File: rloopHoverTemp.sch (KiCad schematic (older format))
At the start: 26 parts, among them P1 CONN_01X02, P2 CONN_01X02, P3 CONN_01X01, P4 CONN_01X01, Q1 Q_NPN_BEC, Q2 Q_NPN_BEC, U1 XTR117, U2 TS305-10C50, U3 LTC2054, U4 XTR117, U5 LTC2054

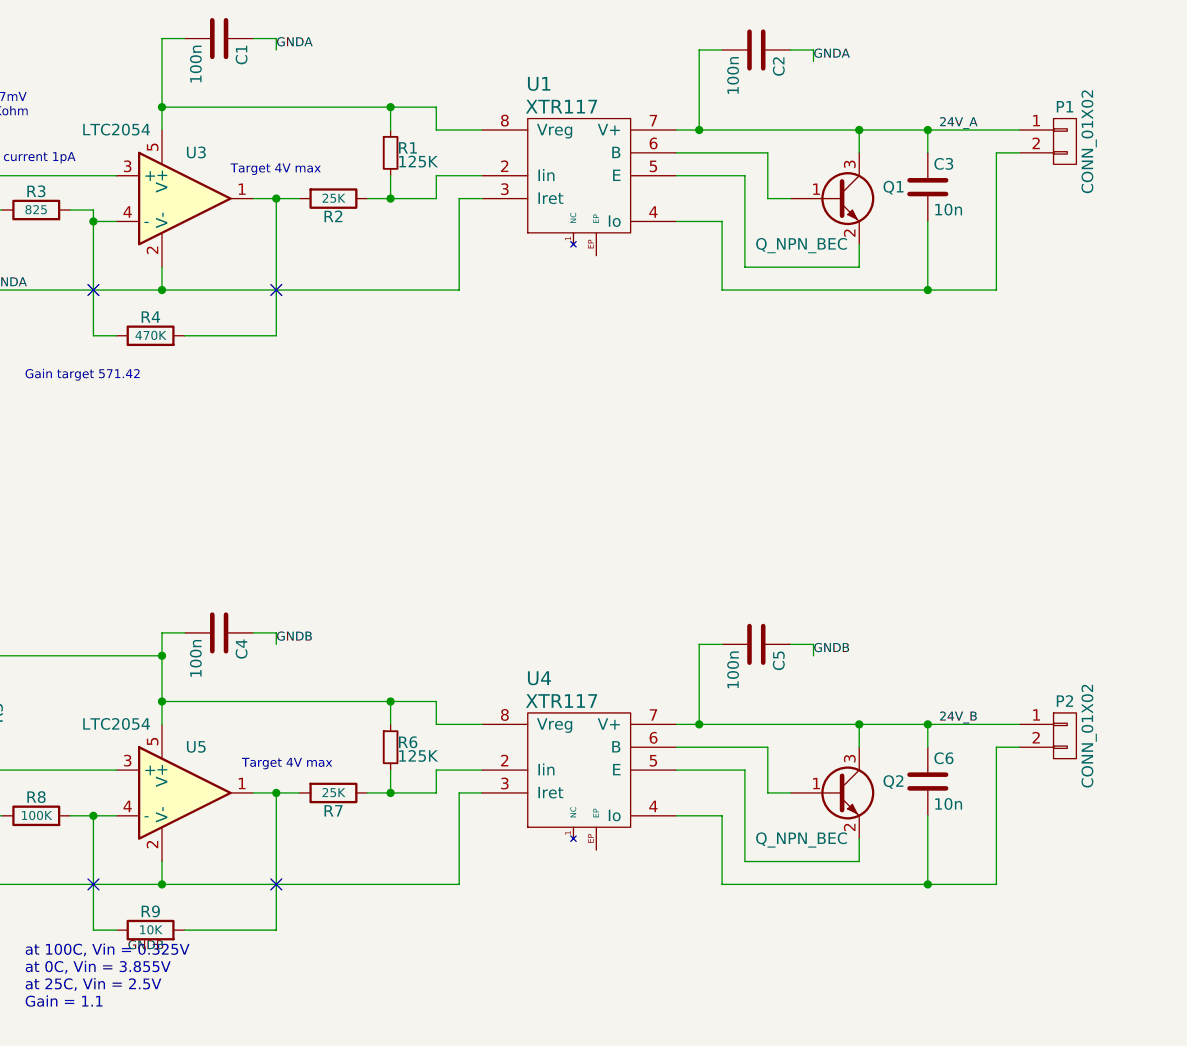
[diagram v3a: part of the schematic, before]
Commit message: added reverse wiring protection diode
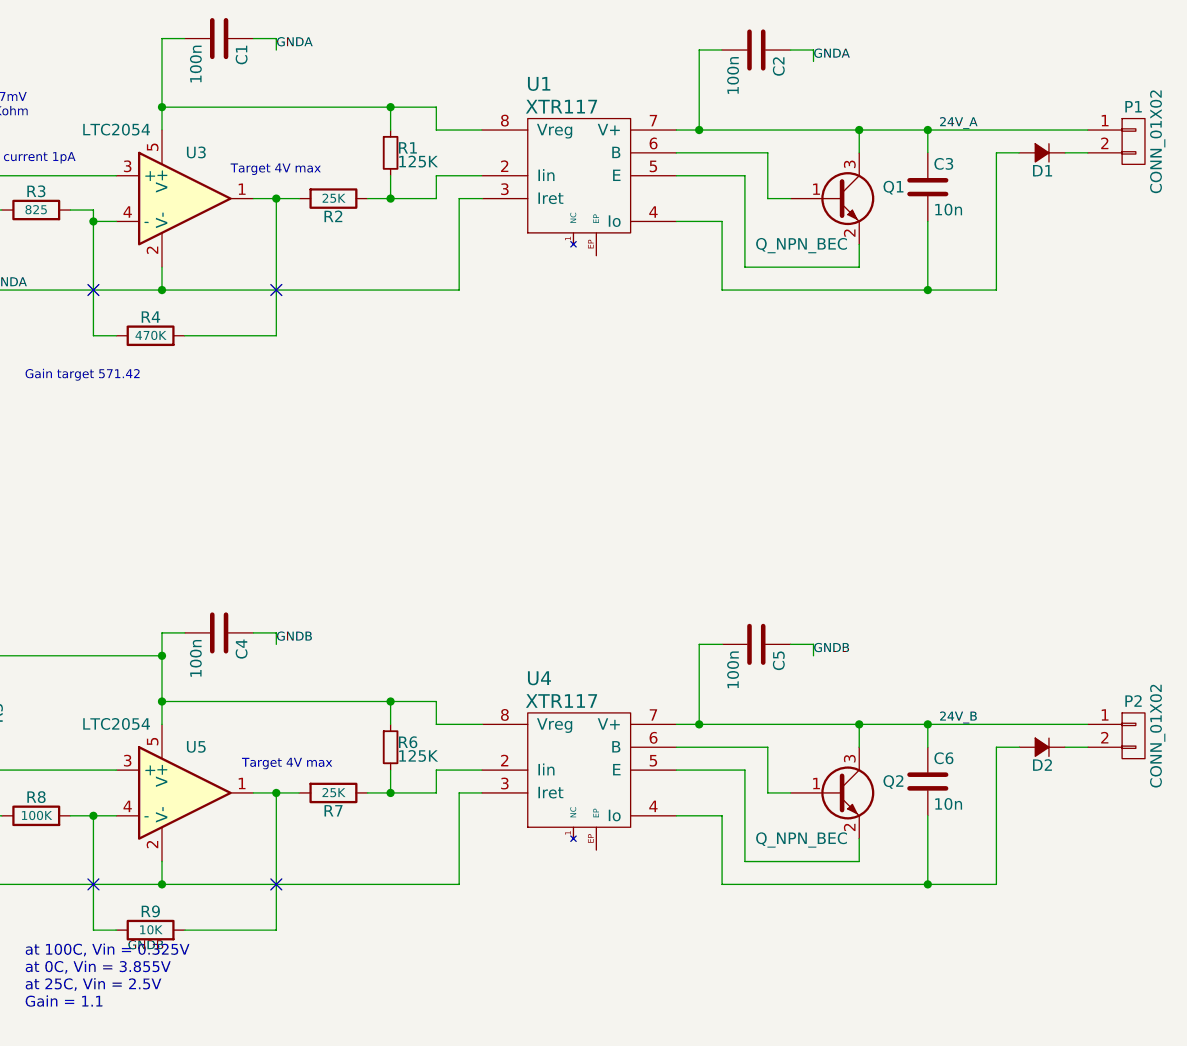
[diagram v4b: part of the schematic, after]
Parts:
- added D1, D2: D_Small, -footprints:SOD-323, symbol D_Small
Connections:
- net at C3.2, U1.4 (Io): now also D1.2 (A); no longer P1.2 (P2)
- net at C6.2, U4.4 (Io): now also D2.2 (A); no longer P2.2 (P2)
- new net: D1.1 (K), P1.2 (P2)
- new net: D2.1 (K), P2.2 (P2)
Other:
- moved on the sheet: P1, P2
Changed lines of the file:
@@
 L CONN_01X02 P1
 U 1 1 573A93C7
-P 8450 1500
-F 0 "P1" H 8450 1650 50  0000 C CNN
-F 1 "CONN_01X02" V 8550 1500 50  0000 C CNN
-F 2 "-footprints:CONN-JST-XH-2-PTH-RGT" H 8450 1500 50  0001 C CNN
-F 3 "" H 8450 1500 50  0000 C CNN
-	1    8450 1500
+P 8750 1500
+F 0 "P1" H 8750 1650 50  0000 C CNN
+F 1 "CONN_01X02" V 8850 1500 50  0000 C CNN
+F 2 "-footprints:CONN-JST-XH-2-PTH-RGT" H 8750 1500 50  0001 C CNN
+F 3 "" H 8750 1500 50  0000 C CNN
+	1    8750 1500
 	1    0    0    -1
 $EndComp
@@
 L CONN_01X02 P2
 U 1 1 573AC4EB
-P 8450 4100
-F 0 "P2" H 8450 4250 50  0000 C CNN
-F 1 "CONN_01X02" V 8550 4100 50  0000 C CNN
-F 2 "-footprints:CONN-JST-XH-2-PTH-RGT" H 8450 4100 50  0001 C CNN
-F 3 "" H 8450 4100 50  0000 C CNN
-	1    8450 4100
+P 8750 4100
+F 0 "P2" H 8750 4250 50  0000 C CNN
+F 1 "CONN_01X02" V 8850 4100 50  0000 C CNN
+F 2 "-footprints:CONN-JST-XH-2-PTH-RGT" H 8750 4100 50  0001 C CNN
+F 3 "" H 8750 4100 50  0000 C CNN
+	1    8750 4100
 	1    0    0    -1
 $EndComp
@@
 	5900 1450 5700 1450
 Wire Wire Line
-	5700 1350 5700 1450
-Wire Wire Line
-	4500 1350 5700 1350
+	5700 1450 5700 1350
+Wire Wire Line
+	5700 1350 4500 1350
 Wire Wire Line
 	4500 1050 4500 1450
@@
 	5800 1750 5900 1750
 Wire Wire Line
-	6750 1450 8250 1450
+	6750 1450 8550 1450
 Wire Wire Line
 	7250 1750 7150 1750
@@
 	8250 1550 8150 1550
 Wire Wire Line
-	8150 2150 8150 1550
-Wire Wire Line
-	6950 2150 8150 2150
+	8150 1550 8150 2150
+Wire Wire Line
+	8150 2150 6950 2150
 Wire Wire Line
 	6950 2150 6950 1850
@@
 	5900 4050 5700 4050
 Wire Wire Line
-	5700 3950 5700 4050
-Wire Wire Line
-	4500 3950 5700 3950
+	5700 4050 5700 3950
+Wire Wire Line
+	5700 3950 4500 3950
 Wire Wire Line
 	4500 3650 4500 4050
@@
 	5800 4350 5900 4350
 Wire Wire Line
-	6750 4050 8250 4050
+	6750 4050 8550 4050
 Wire Wire Line
 	7250 4350 7150 4350
@@
 	8250 4150 8150 4150
 Wire Wire Line
-	8150 4750 8150 4150
-Wire Wire Line
-	6950 4750 8150 4750
+	8150 4150 8150 4750
+Wire Wire Line
+	8150 4750 6950 4750
 Wire Wire Line
 	6950 4750 6950 4450
@@
 Text Label 3450 4750 0    39   ~ 0
 GNDB
+$Comp
+L D_Small D1
+U 1 1 573B860C
+P 8350 1550
+F 0 "D1" H 8300 1630 50  0000 L CNN
+F 1 "D_Small" H 8200 1470 50  0001 L CNN
+F 2 "-footprints:SOD-323" V 8350 1550 50  0001 C CNN
+F 3 "" V 8350 1550 50  0000 C CNN
+	1    8350 1550
+	-1   0    0    1
+$EndComp
+Wire Wire Line
+	8550 1550 8450 1550
+$Comp
+L D_Small D2
+U 1 1 573B8C6E
+P 8350 4150
+F 0 "D2" H 8300 4230 50  0000 L CNN
+F 1 "D_Small" H 8200 4070 50  0001 L CNN
+F 2 "-footprints:SOD-323" V 8350 4150 50  0001 C CNN
+F 3 "" V 8350 4150 50  0000 C CNN
+	1    8350 4150
+	-1   0    0    1
+$EndComp
+Wire Wire Line
+	8550 4150 8450 4150
 $EndSCHEMATC

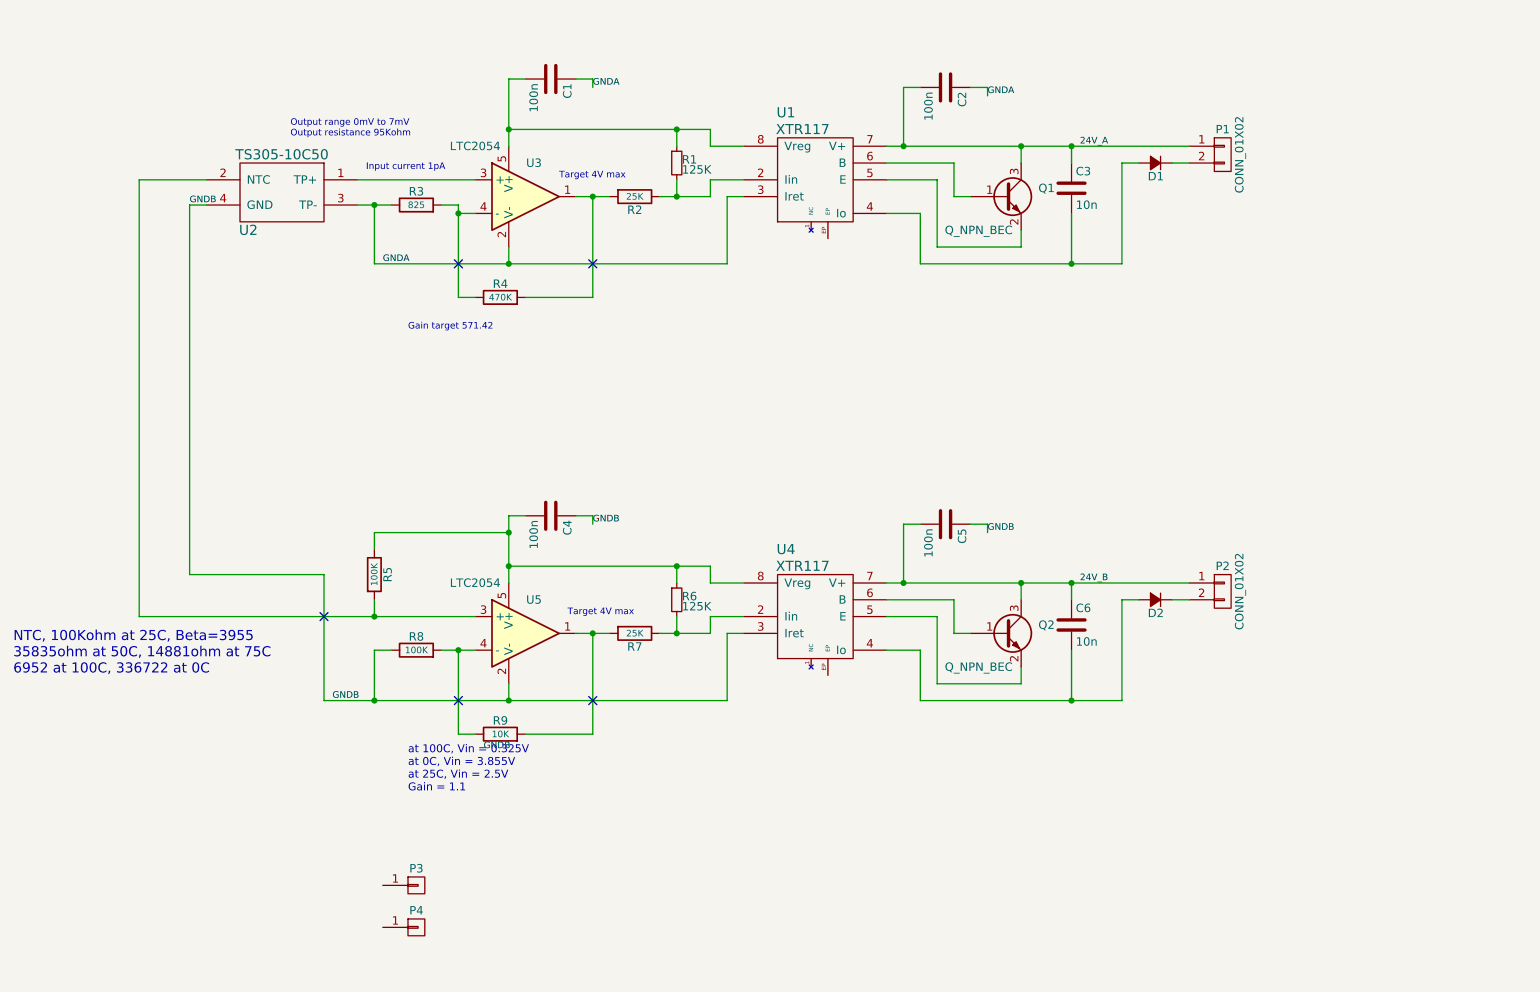
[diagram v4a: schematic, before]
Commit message: complete redo with MLX sensor
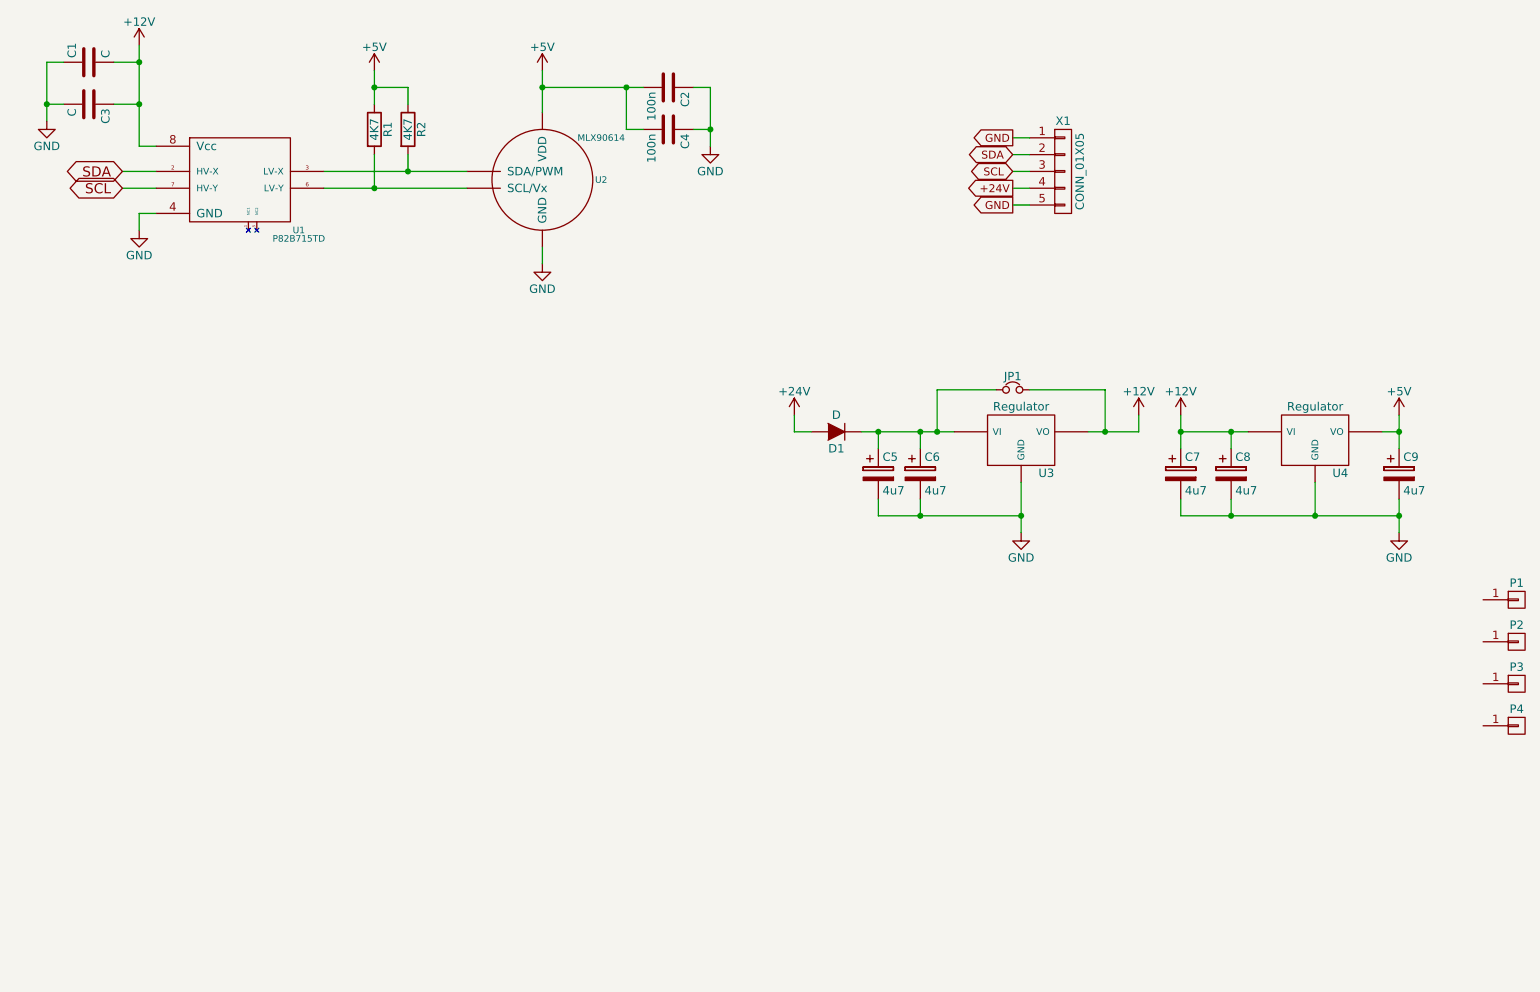
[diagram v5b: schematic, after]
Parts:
- removed C5: 100n, Capacitors_SMD:C_0603, symbol C
- removed C6: 10n, Capacitors_SMD:C_0603, symbol C
- removed D1, D2: D_Small, -footprints:SOD-323, symbol D_Small
- removed P1, P2: CONN_01X02, -footprints:CONN-JST-XH-2-PTH-RGT, symbol CONN_01X02
- removed Q1, Q2: Q_NPN_BEC, TO_SOT_Packages_SMD:SOT-23, symbol Q_NPN_BEC
- removed R1, R6: 125K, Resistors_SMD:R_0603_HandSoldering, symbol R_Small
- removed R3: 825, Resistors_SMD:R_0603_HandSoldering, symbol R
- removed R4: 470K, Resistors_SMD:R_0603_HandSoldering, symbol R
- removed R5, R8: 100K, Resistors_SMD:R_0603_HandSoldering, symbol R
- removed R7: 25K, Resistors_SMD:R_0603_HandSoldering, symbol R
- removed R9: 10K, Resistors_SMD:R_0603_HandSoldering, symbol R
- removed U1, U4: XTR117, Housings_SSOP:MSOP-8_3x3mm_Pitch0.65mm, symbol XTR117
- removed U2: TS305-10C50, -footprints:TS305-10C50, symbol TS305-10C50
- removed U3, U5: LTC2054, TO_SOT_Packages_SMD:SOT-23-5, symbol MCP6001
- added C5, C6, C7, C8, C9: 4u7, Capacitors_SMD:C_1206_HandSoldering, symbol CP
- added D1: D, Diodes_SMD:SOD-123, symbol D
- added JP1: Jumper_NC_Small, -footprints:SOLDERJUMPER, symbol Jumper_NC_Small
- added P1, P2: CONN_01X01, -footprints:SCREWPAD-4-40, symbol CONN_01X01
- added R1: 4K7, Resistors_SMD:R_0603_HandSoldering, symbol R
- added U1: P82B715TD, Housings_SOIC:SOIC-8_3.9x4.9mm_Pitch1.27mm, symbol P82B715TD
- added U2: MLX90614, -footprints:TO39, symbol MLX90614
- added U3, U4: Regulator, -footprints:SOT89-3-VREG, symbol Regulator
- added X1: CONN_01X05, Pin_Headers:Pin_Header_Angled_1x05, symbol CONN_01X05
- C1: value 100n -> C; footprint Capacitors_SMD:C_0603 -> Capacitors_SMD:C_0603_HandSoldering
- C2, C4: footprint Capacitors_SMD:C_0603 -> Capacitors_SMD:C_0603_HandSoldering
- C3: value 10n -> C; footprint Capacitors_SMD:C_0603 -> Capacitors_SMD:C_0603_HandSoldering
- R2: value 25K -> 4K7
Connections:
- net GNDA is gone; now on net GND: C1.1, C2.1
- net GNDB is gone; now on net GND: C4.1
- net +5V: now reaches R2.1
- net +5V: now also C2.2, C4.2, C9.1, R1.1, U2.3 (VDD), U4.VO
- net GND: now reaches C3.2
- net GND: now also C5.2, C6.2, C7.2, C8.2, C9.2, U1.4 (GND), U2.4 (GND), U3.GND, U4.GND, X1.1 (P1), X1.5 (P5)
- net +12V: now reaches C1.2
- net +12V: now also C3.1, C7.1, C8.1, JP1.2, U1.8 (Vcc), U3.VO, U4.VI
- net at R2.2: now also U1.3 (LV-X), U2.2 (SDA/PWM)
- removed net 24V_A: C2.2, C3.1
- new net: R1.2, U1.6 (LV-Y), U2.1 (SCL/Vx)
- new net: C5.1, C6.1, D1.1 (K), JP1.1, U3.VI
- new net +24V: D1.2 (A), X1.4 (P4)
- new net SCL: U1.7 (HV-Y), X1.3 (P3)
- new net SDA: U1.2 (HV-X), X1.2 (P2)
- no-connect marks 5 -> 0
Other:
- note removed: "Gain target 571.42"
- note removed: "Input current 1pA"
- note removed: "NTC, 100Kohm at 25C, Beta=3955\n35835ohm at 50C, 14881ohm at 75C\n6952 at 100C, 336722 at 0C"
- note removed: "Output range 0mV to 7mV\nOutput resistance 95Kohm"
- note removed: "Target 4V max"
- note removed: "at 100C, Vin = 0.325V\nat 0C, Vin = 3.855V\nat 25C, Vin = 2.5V\nGain = 1.1"
